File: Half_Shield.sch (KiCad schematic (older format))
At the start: 34 parts

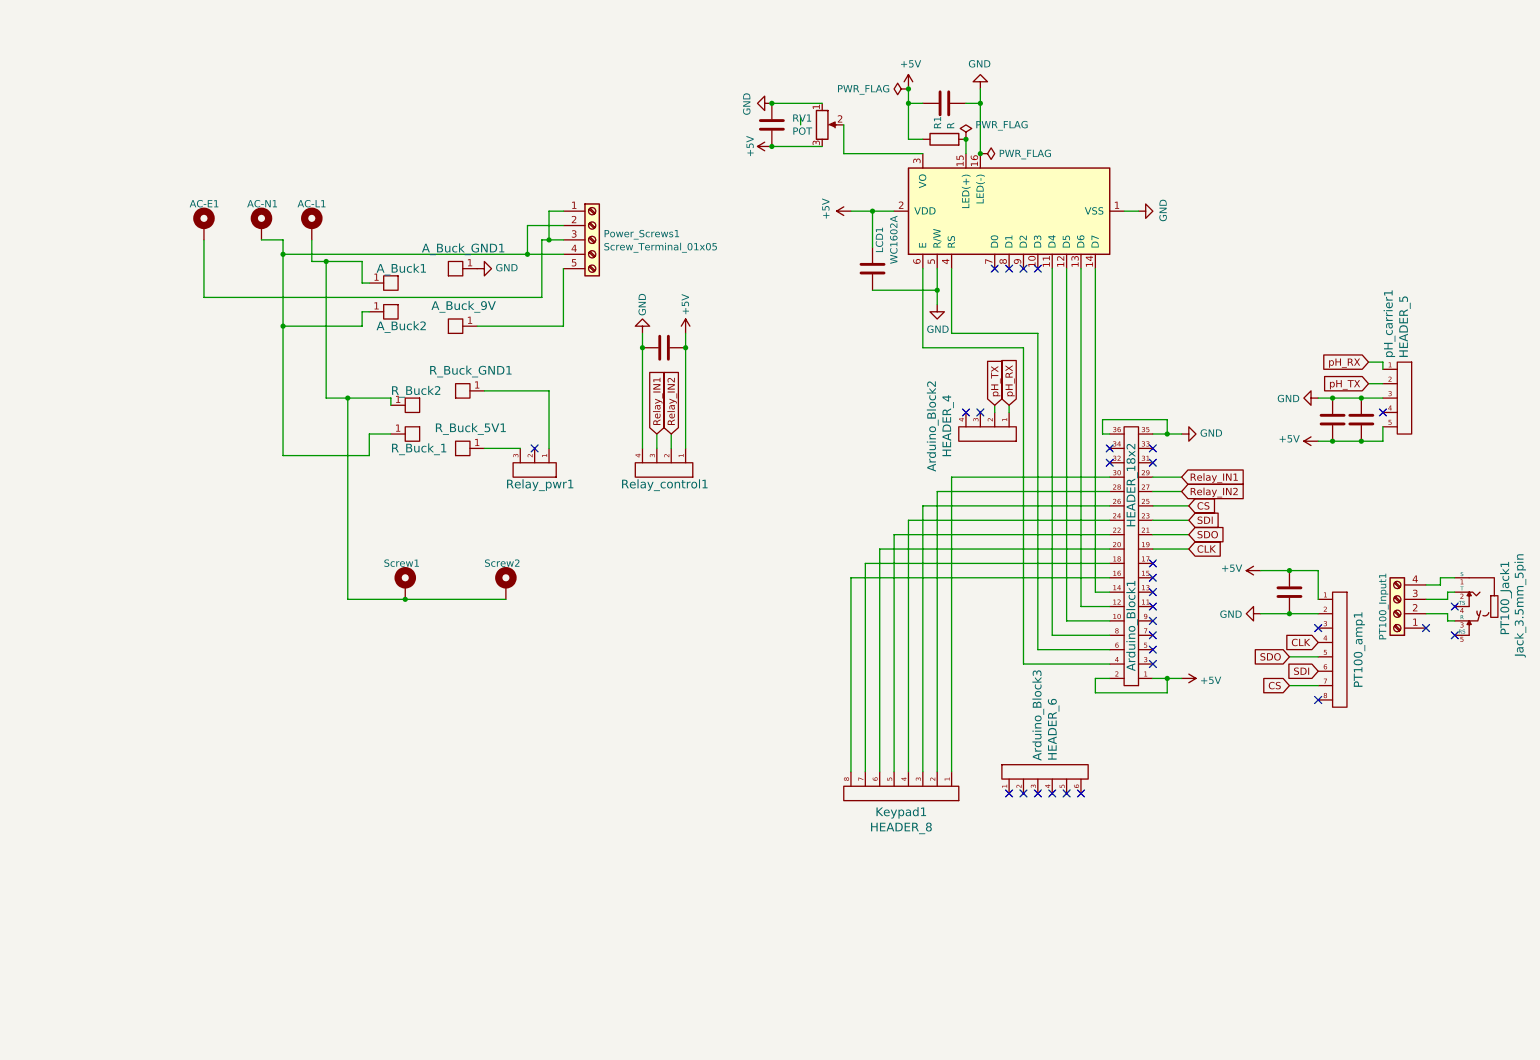
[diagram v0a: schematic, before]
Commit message: adding RTC and switching power supply, rewiring
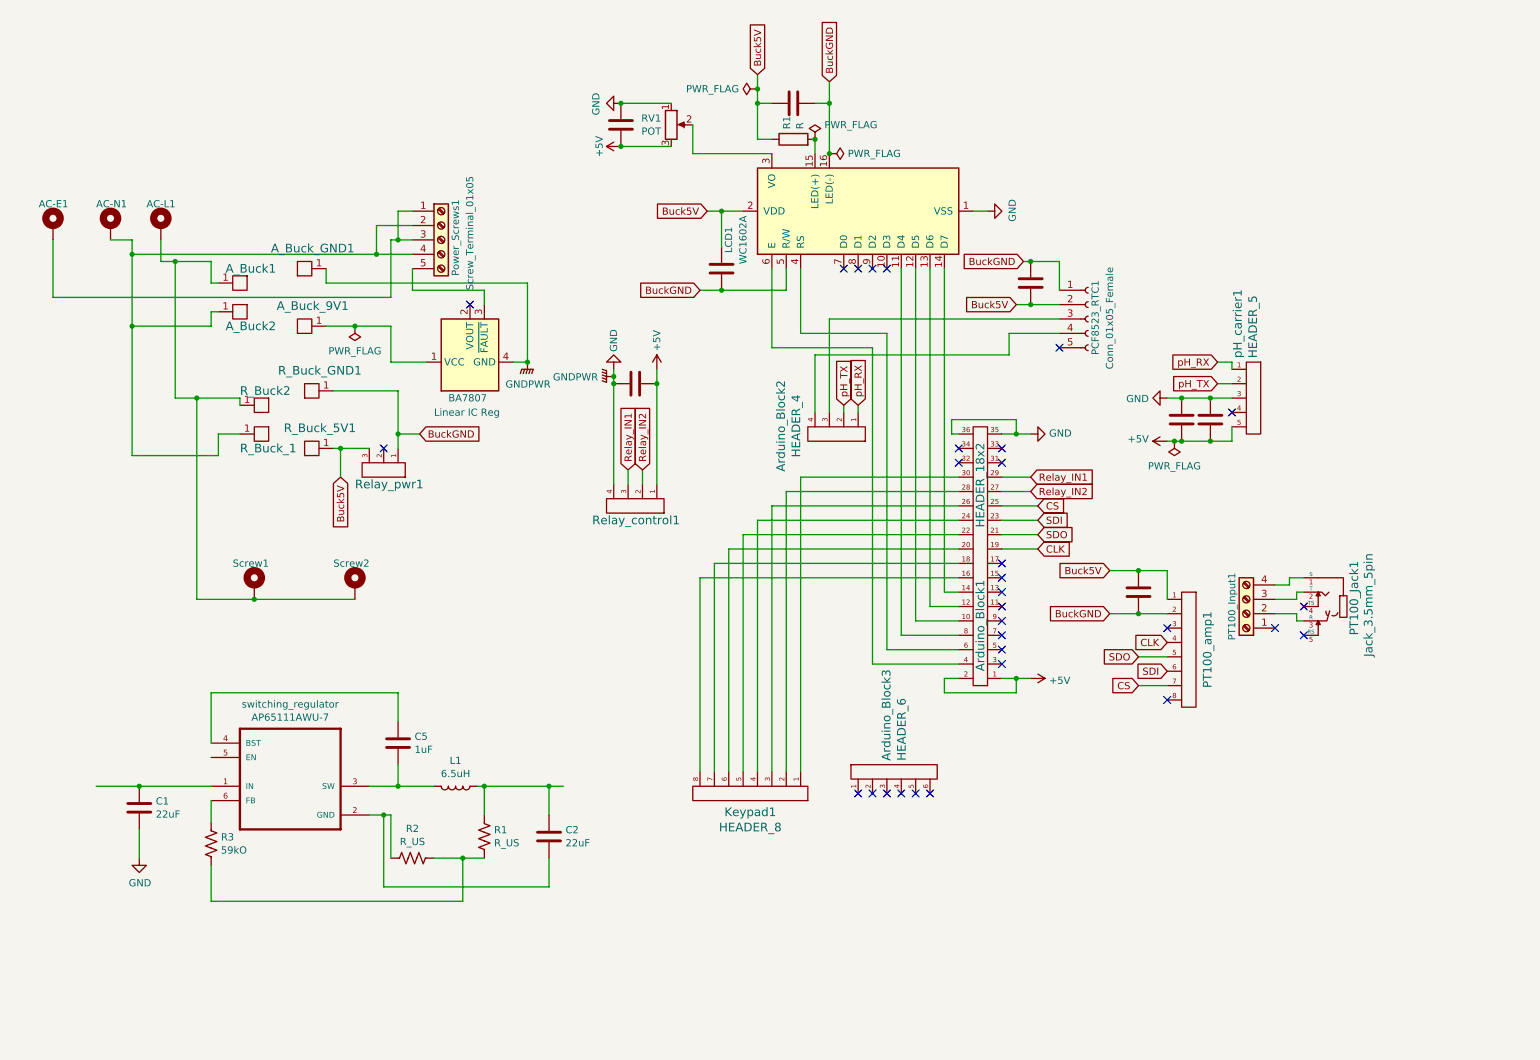
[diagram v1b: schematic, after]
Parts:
- added BA7807: Linear IC Reg, TO_SOT_Packages_SMD:TO-252-3_TabPin4, symbol Sensor_Current:A1365xKTTN-1
- added C1, C2: 22uF, symbol Device:C
- added C5: 1uF, symbol Device:C
- added C8: C-device, Capacitors_SMD:C_0805, symbol Half_Shield-rescue:C-device
- added L1: 6.5uH, symbol Device:L
- added PCF8523_RTC1: Conn_01x05_Female, Pin_Headers:Pin_Header_Straight_1x05_Pitch2.54mm, symbol Connector:Conn_01x05_Female
- added R1, R2: R_US, symbol Device:R_US
- added R3: 59kO, symbol Device:R_US
- added switching_regulator: AP65111AWU-7, SOT95P280X100-6N, symbol AP65111AWU-7:AP65111AWU-7
- RV1: footprint Potentiometers:Potentiometer_Bourns_PTV09A-2_Vertical -> Potentiometers:Potentiometer_Trimmer_Vishay_T73YP_Horizontal
- renumbered A_Buck_9V to A_Buck_9V1
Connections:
- net +5V: no longer C2.2, C4.1, C5.2, LCD1.2 (VDD), PT100_amp1.1, R1.1
- net GND: now also BA7807.4 (GND), C1.2; no longer C2.1, C4.2, C5.1, LCD1.16 (LED(-)), LCD1.5 (R/W), PT100_amp1.2
- net at Arduino_Block2.3: now also PCF8523_RTC1.3 (Pin_3)
- net at Arduino_Block2.4: now also PCF8523_RTC1.4 (Pin_4)
- net BuckGND: now reaches R_Buck_GND1.1, Relay_pwr1.1
- net BuckGND: now also C2.1, C4.2, C5.1, LCD1.16 (LED(-)), LCD1.5 (R/W), PT100_amp1.2, C8.1, PCF8523_RTC1.1 (Pin_1)
- net Buck5V: now reaches R_Buck_5V1.1, Relay_pwr1.3
- net Buck5V: now also C2.2, C4.1, C5.2, LCD1.2 (VDD), PT100_amp1.1, R1.1, C8.2, PCF8523_RTC1.2 (Pin_2)
- net at A_Buck_9V1.1: now also BA7807.1 (VCC); no longer Power_Screws1.5 (Pin_5)
- new net: BA7807.3 (~FAULT), Power_Screws1.5 (Pin_5)
- new net: C1.1, switching_regulator.1 (IN)
- new net: C2.2, R2.2, switching_regulator.2 (GND)
- new net: C5.2, L1.2, switching_regulator.3 (SW)
- new net: C5.1, switching_regulator.4 (BST)
- new net: R3.1, switching_regulator.6 (FB)
- new net: R1.2, R2.1, R3.2
- new net: C2.1, L1.1, R1.1
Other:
- moved on the sheet: AC-E1, AC-L1, AC-N1, A_Buck1, A_Buck2, A_Buck_9V1, A_Buck_GND1, Arduino_Block1, Arduino_Block2, Arduino_Block3, Keypad1, LCD1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

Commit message: 100k ohm resistor on EN to IN
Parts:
- added R?: 100k, symbol Device:R_US
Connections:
- net at C1.1, switching_regulator.1 (IN): now also R?.2
- net at switching_regulator.5 (EN): now also R?.1
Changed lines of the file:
@@
 $EndComp
 Wire Wire Line
-	1950 5800 1450 5800
+	1950 5800 1550 5800
 Wire Wire Line
 	1450 6100 1450 6300
@@
 Wire Wire Line
 	3150 6000 3200 6000
+$Comp
+L Device:R_US R?
+U 1 1 5C7BAE0F
+P 1700 5600
+F 0 "R?" V 1495 5600 50  0000 C CNN
+F 1 "100k" V 1586 5600 50  0000 C CNN
+F 2 "" V 1740 5590 50  0001 C CNN
+F 3 "~" H 1700 5600 50  0001 C CNN
+	1    1700 5600
+	0    1    1    0
+$EndComp
+Wire Wire Line
+	1950 5600 1850 5600
+Wire Wire Line
+	1550 5600 1550 5800
+Connection ~ 1550 5800
+Wire Wire Line
+	1550 5800 1450 5800
 $EndSCHEMATC

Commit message: first attempt at buck converter
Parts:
- removed BA7807: Linear IC Reg, TO_SOT_Packages_SMD:TO-252-3_TabPin4, symbol Sensor_Current:A1365xKTTN-1
- removed C1, C2: 22uF, symbol Device:C
- removed C5: 1uF, symbol Device:C
- removed R1, R2: R_US, symbol Device:R_US
- removed R3: 59kO, symbol Device:R_US
- removed R?: 100k, symbol Device:R_US
- removed switching_regulator: AP65111AWU-7, SOT95P280X100-6N, symbol AP65111AWU-7:AP65111AWU-7
- added Cbst1: 100nF, Capacitors_SMD:C_0603, symbol Device:C
- added Cin1: 22uF, Capacitors_SMD:C_0805, symbol Device:C
- added Cout1: 47uF, Capacitors_SMD:C_1206, symbol Device:C
- added Rfbb1: 10kOhm, Resistors_SMD:R_0201, symbol Device:R_US
- added Rfbt1: 82.5kOhm, Resistors_SMD:R_0402, symbol Device:R_US
- added U1: TPS561208DDC, SOT95P280X110-6N:SOT95P280X110-6N, symbol Half_Shield_parts:TPS561208DDC
- L1: value 6.5uH -> 4.7uH; footprint (none) -> Bourns_Inductor_Footprint:SRN6045-4R7Y
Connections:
- net +5V: now also C2.2, C4.1, C5.2, C8.2, LCD1.2 (VDD), PCF8523_RTC1.2 (Pin_2), PT100_amp1.1, R1.1
- net GND: now also C2.1, C4.2, C5.1, C8.1, LCD1.16 (LED(-)), LCD1.5 (R/W), PCF8523_RTC1.1 (Pin_1), PT100_amp1.2; no longer A_Buck_GND1.1
- net at A_Buck_9V1.1: now also Cin1.1, U1.3 (VIN), U1.5 (EN)
- net at Power_Screws1.5 (Pin_5): now also L1.1, Cout1.1, Rfbt1.1
- net at L1.2: now also Cbst1.1, U1.2 (SW)
- removed net Buck5V: C2.2, C4.1, C5.2, C8.2, LCD1.2 (VDD), PCF8523_RTC1.2 (Pin_2), PT100_amp1.1, R1.1, R_Buck_5V1.1, Relay_pwr1.3
- removed net BuckGND: C2.1, C4.2, C5.1, C8.1, LCD1.16 (LED(-)), LCD1.5 (R/W), PCF8523_RTC1.1 (Pin_1), PT100_amp1.2, R_Buck_GND1.1, Relay_pwr1.1
- new net: R_Buck_GND1.1, Relay_pwr1.1
- new net: R_Buck_5V1.1, Relay_pwr1.3
- new net: A_Buck_GND1.1, Cin1.2, Cout1.2, Rfbb1.2, U1.1 (GND)
- new net: Rfbb1.1, Rfbt1.2, U1.4 (VFB)
- new net: Cbst1.2, U1.6 (VBST)
- no-connect marks 31 -> 30

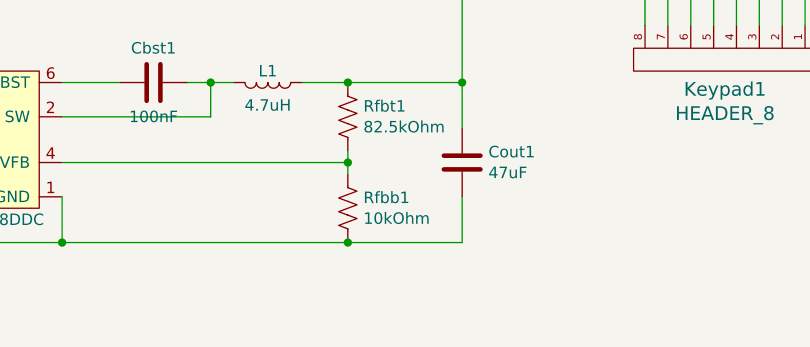
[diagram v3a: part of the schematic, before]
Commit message: grounded switching regulator circuit and other small modifications
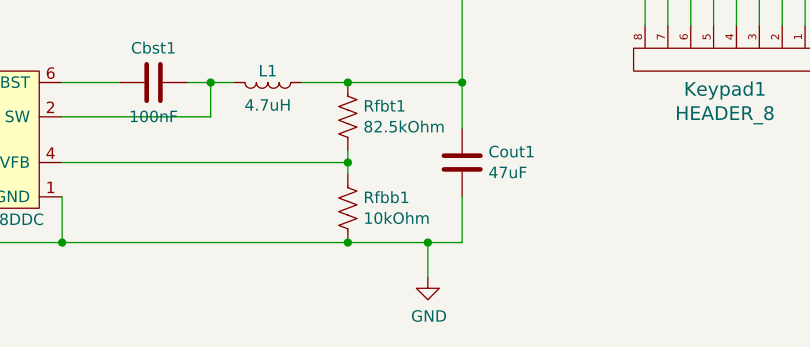
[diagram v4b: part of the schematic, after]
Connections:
- net GND: now also A_Buck_GND1.1, Cin1.2, Cout1.2, Rfbb1.2, U1.1 (GND)
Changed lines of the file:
@@
 F 1 "TPS561208DDC" H 2450 5850 50  0000 C CNN
 F 2 "SOT95P280X110-6N:SOT95P280X110-6N" H 2450 6200 50  0001 C CNN
-F 3 "" H 2450 6200 50  0001 C CNN
+F 3 "http://www.ti.com/lit/ds/symlink/tps561208.pdf" H 2450 6200 50  0001 C CNN
 	1    2450 6200
 	1    0    0    -1
@@
 Connection ~ 4050 5950
 Wire Wire Line
-	4050 6650 4550 6650
+	4050 6650 4400 6650
 Wire Wire Line
 	4550 6650 4550 6450
@@
 Wire Wire Line
 	2800 3450 3050 3450
+$Comp
+L power:GND #PWR0110
+U 1 1 5C8B522B
+P 4400 6800
+F 0 "#PWR0110" H 4400 6550 50  0001 C CNN
+F 1 "GND" H 4405 6627 50  0000 C CNN
+F 2 "" H 4400 6800 50  0001 C CNN
+F 3 "" H 4400 6800 50  0001 C CNN
+	1    4400 6800
+	1    0    0    -1
+$EndComp
+Wire Wire Line
+	4400 6650 4400 6800
+Connection ~ 4400 6650
+Wire Wire Line
+	4400 6650 4550 6650
 $EndSCHEMATC

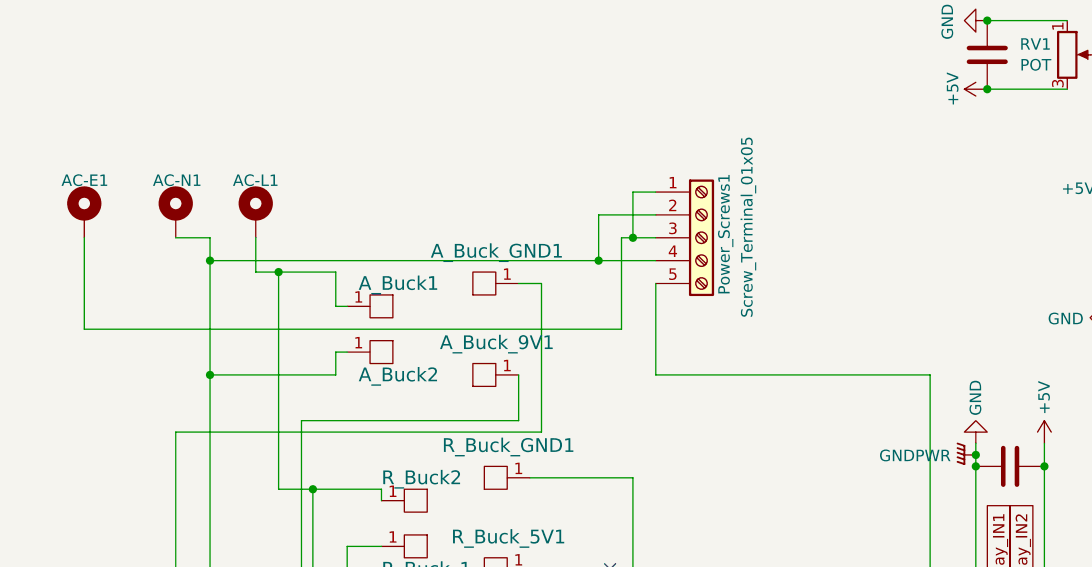
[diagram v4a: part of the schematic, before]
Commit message: finalizing switching regulator circuit
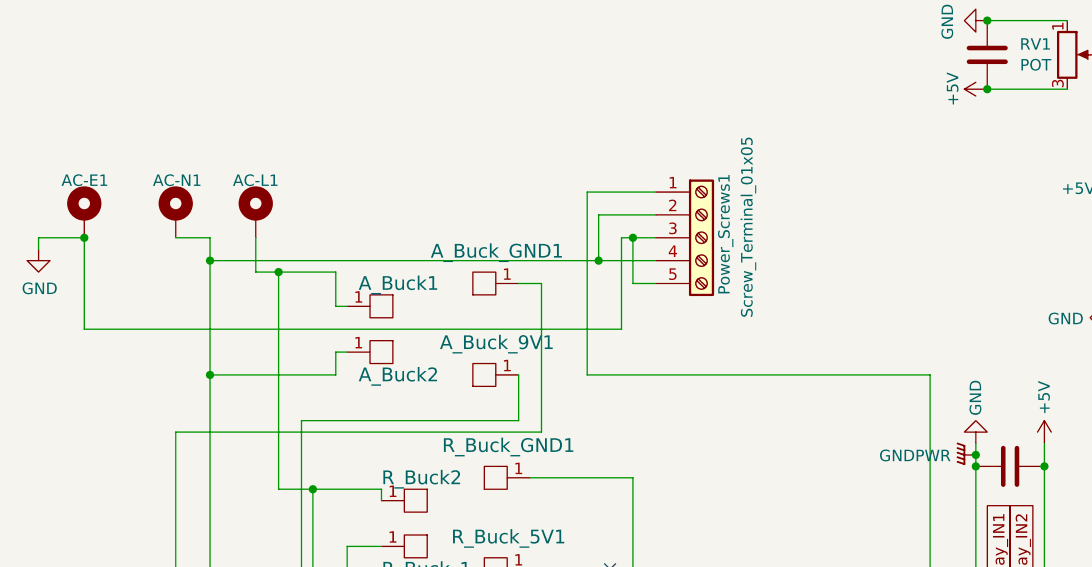
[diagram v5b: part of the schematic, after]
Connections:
- net GND: now also AC-E1.1, Power_Screws1.3 (Pin_3), Power_Screws1.5 (Pin_5)
- net at Cout1.1, L1.1, Rfbt1.1: now also Power_Screws1.1 (Pin_1); no longer Power_Screws1.5 (Pin_5)
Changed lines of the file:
@@
 Wire Wire Line
 	3200 2400 850  2400
-Wire Wire Line
-	3350 1800 3250 1800
-Wire Wire Line
-	3250 1800 3250 2000
 Connection ~ 3250 2000
 Wire Wire Line
@@
 Connection ~ 2800 6650
 Wire Wire Line
-	3350 2200 3350 2600
-Wire Wire Line
-	3350 2600 4550 2600
-Wire Wire Line
 	4550 2600 4550 5950
 Connection ~ 4550 5950
@@
 Wire Wire Line
 	4400 6650 4550 6650
+$Comp
+L power:GND #PWR0111
+U 1 1 5C8F371B
+P 650 2050
+F 0 "#PWR0111" H 650 1800 50  0001 C CNN
+F 1 "GND" H 655 1877 50  0000 C CNN
+F 2 "" H 650 2050 50  0001 C CNN
+F 3 "" H 650 2050 50  0001 C CNN
+	1    650  2050
+	1    0    0    -1
+$EndComp
+Wire Wire Line
+	850  2000 650  2000
+Wire Wire Line
+	650  2000 650  2050
+Connection ~ 850  2000
+Wire Wire Line
+	3350 2200 3250 2200
+Wire Wire Line
+	3250 2200 3250 2000
+Wire Wire Line
+	3350 1800 3050 1800
+Wire Wire Line
+	3050 1800 3050 2600
+Wire Wire Line
+	3050 2600 4550 2600
 $EndSCHEMATC

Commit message: small fix to pcb
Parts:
- Rfbb1: footprint Resistors_SMD:R_0201 -> Resistors_SMD:R_0805
- Rfbt1: footprint Resistors_SMD:R_0402 -> Resistors_SMD:R_0805
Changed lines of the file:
@@
 F 0 "Rfbt1" H 4118 6146 50  0000 L CNN
 F 1 "82.5kOhm" H 4118 6055 50  0000 L CNN
-F 2 "Resistors_SMD:R_0402" V 4090 6090 50  0001 C CNN
+F 2 "Resistors_SMD:R_0805" V 4090 6090 50  0001 C CNN
 F 3 "~" H 4050 6100 50  0001 C CNN
 	1    4050 6100
@@
 F 0 "Rfbb1" H 4118 6546 50  0000 L CNN
 F 1 "10kOhm" H 4118 6455 50  0000 L CNN
-F 2 "Resistors_SMD:R_0201" V 4090 6490 50  0001 C CNN
+F 2 "Resistors_SMD:R_0805" V 4090 6490 50  0001 C CNN
 F 3 "~" H 4050 6500 50  0001 C CNN
 	1    4050 6500
